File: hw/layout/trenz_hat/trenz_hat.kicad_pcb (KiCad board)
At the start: 2 copper layers, 87 parts

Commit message: Expose Trenz GPIOs on the Pi-outline HDI sensor HAT
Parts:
- added J86: , elec:TZ_FFC40, F.Cu at (0.00, 0.00)
- added J87: , elec:TZ_FFC40, F.Cu at (10.0, 0.00)
- added J88: , elec:TZ_FFC60, F.Cu at (20.0, 0.00)
- added J89: , elec:TZ_FFC60, F.Cu at (30.0, 0.00)
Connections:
- J80 pad 100: 100 -> FPGA_B14_L24_N
- J80 pad 11: GND -> 11
- J80 pad 15: 15 -> FPGA_B13_L6_N
- J80 pad 17: 17 -> FPGA_B13_L6_P
- J80 pad 18: 18 -> FPGA_B13_L3_P
- J80 pad 20: 20 -> FPGA_B13_L3_N
- J80 pad 21: 21 -> FPGA_B13_L5_N
- J80 pad 22: 22 -> FPGA_B13_L11_N
- J80 pad 23: 23 -> FPGA_B13_L5_P
- J80 pad 24: 24 -> FPGA_B13_L11_P
- J80 pad 25: 25 -> GND
- J80 pad 26: 26 -> FPGA_B13_L9_N
- J80 pad 28: 28 -> FPGA_B13_L9_P
- J80 pad 32: GND -> FPGA_B16_L22_P
- J80 pad 34: 34 -> FPGA_B16_L22_N
- J80 pad 35: j80-35 -> FPGA_B16_L16_P
- J80 pad 36: j80-36 -> FPGA_B16_L24_N
- J80 pad 37: 37 -> FPGA_B16_L16_N
- J80 pad 38: j80-38 -> FPGA_B16_L24_P
- J80 pad 39: 39 -> FPGA_B16_L19_N
- J80 pad 41: 41 -> FPGA_B16_L19_P
- J80 pad 42: 42 -> FPGA_B16_L23_P
- J80 pad 44: 44 -> FPGA_B16_L23_N
- J80 pad 45: 45 -> FPGA_B16_L17_N
- J80 pad 46: 46 -> FPGA_B16_L15_P
- J80 pad 47: 47 -> FPGA_B16_L17_P
- J80 pad 48: 48 -> FPGA_B16_L15_N
- J80 pad 49: 49 -> FPGA_B16_L18_N
- J80 pad 50: 50 -> FPGA_B16_L20_P
- J80 pad 51: 51 -> FPGA_B16_L18_P
- J80 pad 52: 52 -> FPGA_B16_L20_N
- J80 pad 55: 55 -> FPGA_B16_L9_N
- J80 pad 56: 56 -> FPGA_B16_L21_P
- J80 pad 57: 57 -> FPGA_B16_L9_P
- J80 pad 58: 58 -> FPGA_B16_L21_N
- J80 pad 59: 59 -> FPGA_B16_L7_N
- J80 pad 60: 60 -> FPGA_B16_L13_P
- J80 pad 61: 61 -> FPGA_B16_L7_P
- J80 pad 62: 62 -> FPGA_B16_L13_N
- J80 pad 65: 65 -> FPGA_B16_L11_P
- J80 pad 66: 66 -> FPGA_B16_L14_P
- J80 pad 67: 67 -> FPGA_B16_L11_N
- J80 pad 68: 68 -> FPGA_B16_L14_N
- J80 pad 69: 69 -> FPGA_B16_L10_N
- J80 pad 7: 7 -> GND
- J80 pad 70: 70 -> FPGA_B16_L3_N
- J80 pad 71: 71 -> FPGA_B16_L10_P
- J80 pad 72: 72 -> FPGA_B16_L3_P
- J80 pad 75: 75 -> FPGA_B16_L5_N
- J80 pad 76: 76 -> FPGA_B16_L12_P
- J80 pad 77: 77 -> FPGA_B16_L5_P
- J80 pad 78: 78 -> FPGA_B16_L12_N
- J80 pad 79: 79 -> FPGA_B16_L2_N
- J80 pad 81: 81 -> FPGA_B16_L2_P
- J80 pad 82: 82 -> FPGA_B16_L8_N
- J80 pad 83: 83 -> GND
- J80 pad 84: 84 -> FPGA_B16_L8_P
- J80 pad 85: 85 -> FPGA_B16_L6_N
- J80 pad 86: 86 -> FPGA_B14_L18_N
- J80 pad 87: 87 -> FPGA_B16_L6_P
- J80 pad 88: 88 -> FPGA_B14_L18_P
- J80 pad 91: 91 -> FPGA_B14_L24_P
- J80 pad 92: 92 -> FPGA_B14_L9_P
- J80 pad 93: 93 -> FPGA_B16_L4_N
- J80 pad 94: 94 -> FPGA_B14_L9_N
- J80 pad 95: 95 -> FPGA_B16_L4_P
- J80 pad 96: 96 -> FPGA_B14_L4_P
- J80 pad 97: 97 -> FPGA_B16_L1_N
- J80 pad 98: 98 -> FPGA_B14_L4_N
- J80 pad 99: 99 -> FPGA_B16_L1_P
- J81 pad 20: j81-20 -> 20
- J81 pad 21: j81-21 -> FPGA_B14_L12_P
- J81 pad 22: j81-22 -> FPGA_B14_L14_P
- J81 pad 23: j81-23 -> FPGA_B14_L12_N
- J81 pad 24: j81-24 -> FPGA_B14_L14_N
- J81 pad 25: j81-25 -> FPGA_B14_L11_P
- J81 pad 26: j81-26 -> FPGA_B14_L13_P
- J81 pad 27: 27 -> FPGA_B14_L11_N
- J81 pad 28: j81-28 -> FPGA_B14_L13_N
- J81 pad 29: GND -> 29
- J81 pad 30: GND -> 30
- J81 pad 31: 31 -> FPGA_B15_L9_N
- J81 pad 32: j81-32 -> FPGA_B14_L16_P
- J81 pad 33: 33 -> FPGA_B15_L9_P
- J81 pad 34: j81-34 -> FPGA_B14_L16_N
- J81 pad 35: j81-35 -> FPGA_B15_L8_N
- J81 pad 36: j81-36 -> FPGA_B14_L15_P
- J81 pad 37: j81-37 -> FPGA_B15_L8_P
- J81 pad 38: j81-38 -> FPGA_B14_L15_N
- J81 pad 41: j81-41 -> FPGA_B15_L7_N
- J81 pad 42: j81-42 -> FPGA_B15_L23_P
- J81 pad 43: 43 -> FPGA_B15_L7_P
- J81 pad 44: j81-44 -> FPGA_B15_L23_N
- J81 pad 45: j81-45 -> FPGA_B15_L13_P
- J81 pad 46: j81-46 -> FPGA_B15_L19_P
- J81 pad 47: j81-47 -> FPGA_B15_L13_N
- J81 pad 48: j81-48 -> FPGA_B15_L19_N
- J81 pad 51: j81-51 -> FPGA_B15_L14_P
- J81 pad 52: j81-52 -> FPGA_B15_L11_P
- J81 pad 53: 53 -> FPGA_B15_L14_N
- J81 pad 54: 54 -> FPGA_B15_L11_N
- J81 pad 55: j81-55 -> FPGA_B15_L12_P
- J81 pad 56: j81-56 -> FPGA_B15_L3_P
- J81 pad 57: j81-57 -> FPGA_B15_L12_N
- J81 pad 58: j81-58 -> FPGA_B15_L3_N
- J81 pad 61: j81-61 -> FPGA_B15_L10_N
- J81 pad 62: j81-62 -> FPGA_B15_L17_N
- J81 pad 63: 63 -> FPGA_B15_L10_P
- J81 pad 64: 64 -> FPGA_B15_L17_P
- J81 pad 65: j81-65 -> FPGA_B15_L18_P
- J81 pad 66: j81-66 -> FPGA_B15_L16_P
- J81 pad 67: j81-67 -> FPGA_B15_L18_N
- J81 pad 68: j81-68 -> FPGA_B15_L16_N
- J81 pad 71: j81-71 -> FPGA_B15_L20_P
- J81 pad 72: j81-72 -> FPGA_B15_L1_P
- J81 pad 73: 73 -> FPGA_B15_L20_N
- J81 pad 74: 74 -> FPGA_B15_L1_N
- J81 pad 75: j81-75 -> FPGA_B15_L15_P
- J81 pad 76: j81-76 -> FPGA_B15_L2_N
- J81 pad 77: j81-77 -> FPGA_B15_L15_N
- J81 pad 78: j81-78 -> FPGA_B15_L2_P
- J81 pad 81: j81-81 -> FPGA_B15_L6_N
- J81 pad 82: j81-82 -> FPGA_B15_L4_P
- J81 pad 83: j81-83 -> FPGA_B15_L6_P
- J81 pad 84: j81-84 -> FPGA_B15_L4_N
- J81 pad 85: j81-85 -> FPGA_B15_L21_P
- J81 pad 86: j81-86 -> FPGA_B15_L5_N
- J81 pad 87: j81-87 -> FPGA_B15_L21_N
- J81 pad 88: j81-88 -> FPGA_B15_L5_P
- J81 pad 90: 90 -> FPGA_B15_IO0
- J81 pad 91: j81-91 -> FPGA_B15_L24_N
- J81 pad 93: j81-93 -> FPGA_B15_L24_P
- J81 pad 95: j81-95 -> FPGA_B15_L22_N
- J81 pad 97: j81-97 -> FPGA_B15_L22_P
- J81 pad 99: j81-99 -> FPGA_B15_IO25
- J82 pad 1: 1 -> FPGA_B13_L14_P
- J82 pad 15: j82-15 -> 15
- J82 pad 2: 2 -> FPGA_B13_L17_P
- J82 pad 21: j82-21 -> 21
- J82 pad 22: j82-22 -> 22
- J82 pad 25: j82-25 -> 25
- J82 pad 26: j82-26 -> 26
- J82 pad 27: j82-27 -> 27
- J82 pad 28: j82-28 -> 28
- J82 pad 3: j82-3 -> FPGA_B13_L14_N
- J82 pad 31: j82-31 -> 31
- J82 pad 33: j82-33 -> 33
- J82 pad 34: j82-34 -> 34
- J82 pad 37: j82-37 -> FPGA_B13_L16_P
- J82 pad 38: j82-38 -> FPGA_B13_L10_P
- J82 pad 39: j82-39 -> FPGA_B13_L16_N
- J82 pad 4: 4 -> FPGA_B13_L17_N
- J82 pad 40: j82-40 -> FPGA_B13_L10_N
- J82 pad 41: j82-41 -> FPGA_B13_L1_P
- J82 pad 42: j82-42 -> FPGA_B13_L15_P
- J82 pad 43: j82-43 -> FPGA_B13_L1_N
- J82 pad 44: j82-44 -> FPGA_B13_L15_N
- J82 pad 47: j82-47 -> FPGA_B13_L4_P
- J82 pad 48: j82-48 -> FPGA_B14_L5_P
- J82 pad 49: j82-49 -> FPGA_B13_L4_N
- J82 pad 50: j82-50 -> FPGA_B14_L5_N
- J82 pad 51: j82-51 -> FPGA_B13_L2_N
- J82 pad 52: j82-52 -> FPGA_B14_L20_P
- J82 pad 53: j82-53 -> FPGA_B13_L2_P
- J82 pad 54: j82-54 -> FPGA_B14_L20_N
- J82 pad 55: j82-55 -> 55
- J82 pad 56: j82-56 -> 56
- J82 pad 57: j82-57 -> FPGA_B13_L12_P
- J82 pad 58: j82-58 -> FPGA_B13_L13_P
- J82 pad 59: j82-59 -> FPGA_B13_L12_N
- J82 pad 60: j82-60 -> FPGA_B13_L13_N
- J82 pad 7: j82-7 -> 7
- U11 pad 11: 11 -> u11-11
- U21 pad 18: u21-18 -> 18
- U21 pad 2: u21-2 -> 2

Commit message: Replace T1 GNSS with single Racotech geophone input
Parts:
- removed C24, C26: , elec:Capacitor_SMD__C_0603_1608Metric
- removed C25: , elec:Capacitor_SMD__C_0805_2012Metric
- removed J2: , elec:Connector_Coaxial__U.FL_Hirose_U.FL-R-SMT-1_Vertical
- removed U21: , elec:RF_GPS__ublox_MAX
- added C90: , elec:Capacitor_SMD__C_1206_3216Metric, F.Cu at (50.0, 0.00)
- added C91: , elec:Capacitor_SMD__C_0603_1608Metric, F.Cu at (60.0, 0.00)
- added C92: , elec:Capacitor_SMD__C_0603_1608Metric, F.Cu at (70.0, 0.00)
- added C93: , elec:Capacitor_SMD__C_0805_2012Metric, F.Cu at (120.0, 0.00)
- added C94: , elec:Capacitor_SMD__C_0805_2012Metric, F.Cu at (140.0, 0.00)
- added C95: , elec:Capacitor_SMD__C_0603_1608Metric, F.Cu at (150.0, 0.00)
- added C96: , elec:Capacitor_SMD__C_0603_1608Metric, F.Cu at (160.0, 0.00)
- added D90: , elec:Package_TO_SOT_SMD__SOT-323_SC-70, F.Cu at (20.0, 0.00)
- added J90: , elec:Connector_Phoenix_MC__PhoenixContact_MCV_1,5_3-G-3.81_1x03_P3.81mm_Vertical, F.Cu at (10.0, 0.00)
- added R90: , elec:Resistor_SMD__R_0603_1608Metric, F.Cu at (30.0, 0.00)
- added R91: , elec:Resistor_SMD__R_0603_1608Metric, F.Cu at (40.0, 0.00)
- added R92: , elec:Resistor_SMD__R_0603_1608Metric, F.Cu at (80.0, 0.00)
- added R93: , elec:Resistor_SMD__R_0603_1608Metric, F.Cu at (90.0, 0.00)
- added R94: , elec:Resistor_SMD__R_0603_1608Metric, F.Cu at (100.0, 0.00)
- added R95: , elec:Resistor_SMD__R_0603_1608Metric, F.Cu at (110.0, 0.00)
- added R96: , elec:Resistor_SMD__R_0603_1608Metric, F.Cu at (130.0, 0.00)
- added R97: , elec:Resistor_SMD__R_0603_1608Metric, F.Cu at (170.0, 0.00)
- added U22: , elec:Package_SO__TSSOP-16_4.4x5mm_P0.65mm, F.Cu at (0.00, 0.00)
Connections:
- net PI_GNSS_PPS renamed PI_GEO_DRDY_N
- U42 pad 16: GNSS_PPS -> GEO_DRDY_N

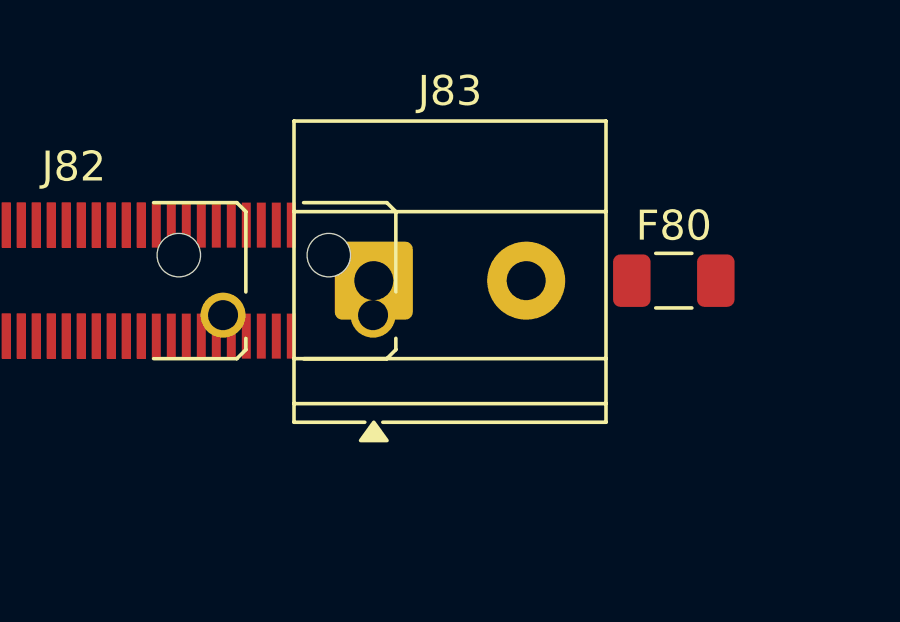
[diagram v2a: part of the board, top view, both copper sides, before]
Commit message: Resolve T1 ribbon clearance with guided flex and windowed support
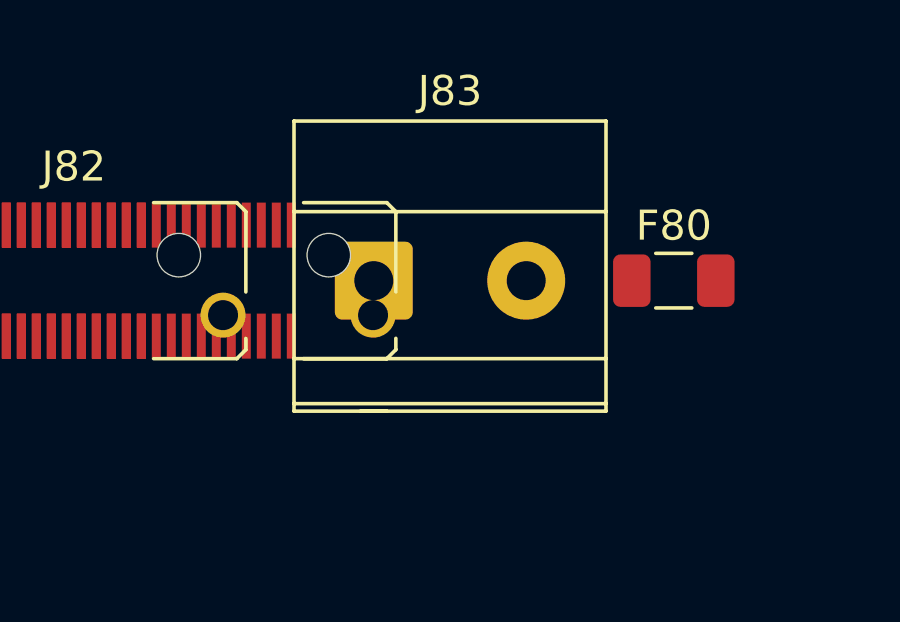
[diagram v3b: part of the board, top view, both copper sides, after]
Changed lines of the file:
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@@
 		)
 		(fp_line
-			(start -2.66 4.72)
-			(end -2.66 -5.32)
-			(stroke
-				(width 0.12)
-				(type solid)
-			)
-			(layer "F.SilkS")
-		)
-		(fp_line
-			(start -0.3 4.72)
-			(end -2.66 4.72)
-			(stroke
-				(width 0.12)
-				(type solid)
-			)
-			(layer "F.SilkS")
-		)
-		(fp_line
-			(start 7.74 -5.32)
-			(end 7.74 4.72)
-			(stroke
-				(width 0.12)
-				(type solid)
-			)
-			(layer "F.SilkS")
-		)
-		(fp_line
-			(start 7.74 4.72)
-			(end 0.3 4.72)
-			(stroke
-				(width 0.12)
-				(type solid)
-			)
-			(layer "F.SilkS")
-		)
-		(fp_line
 			(start -2.54 -5.2)
 			(end 7.62 -5.2)
@@
 			(layer "F.Fab")
 		)
+		(fp_line
+			(start -2.66 4.35)
+			(end -2.66 -5.32)
+			(stroke
+				(width 0.12)
+				(type solid)
+			)
+			(layer "F.SilkS")
+		)
+		(fp_line
+			(start -0.3 4.35)
+			(end -2.66 4.35)
+			(stroke
+				(width 0.12)
+				(type solid)
+			)
+			(layer "F.SilkS")
+		)
+		(fp_line
+			(start 7.74 -5.32)
+			(end 7.74 4.35)
+			(stroke
+				(width 0.12)
+				(type solid)
+			)
+			(layer "F.SilkS")
+		)
+		(fp_line
+			(start 7.74 4.35)
+			(end 0.3 4.35)
+			(stroke
+				(width 0.12)
+				(type solid)
+			)
+			(layer "F.SilkS")
+		)
 		(fp_circle
 			(center 0 0)
@@
 		(fp_poly
 			(pts
-				(xy 0 4.72) (xy 0.44 5.33) (xy -0.44 5.33)
+				(xy 0 4.35) (xy 0.44 4.35) (xy -0.44 4.35)
 			)
 			(stroke
@@
 		)
 		(pad "1" smd roundrect
-			(at -2.8625 -2.275 0)
+			(at -2.8625 -2.275)
 			(size 1.475 0.4)
 			(layers "F.Cu" "F.Mask" "F.Paste")
@@
 		)
 		(pad "2" smd roundrect
-			(at -2.8625 -1.625 0)
+			(at -2.8625 -1.625)
 			(size 1.475 0.4)
 			(layers "F.Cu" "F.Mask" "F.Paste")
@@
 		)
 		(pad "3" smd roundrect
-			(at -2.8625 -0.975 0)
+			(at -2.8625 -0.975)
 			(size 1.475 0.4)
 			(layers "F.Cu" "F.Mask" "F.Paste")
@@
 		)
 		(pad "4" smd roundrect
-			(at -2.8625 -0.325 0)
+			(at -2.8625 -0.325)
 			(size 1.475 0.4)
 			(layers "F.Cu" "F.Mask" "F.Paste")
@@
 		)
 		(pad "5" smd roundrect
-			(at -2.8625 0.325 0)
+			(at -2.8625 0.325)
 			(size 1.475 0.4)
 			(layers "F.Cu" "F.Mask" "F.Paste")
@@
 		)
 		(pad "6" smd roundrect
-			(at -2.8625 0.975 0)
+			(at -2.8625 0.975)
 			(size 1.475 0.4)
 			(layers "F.Cu" "F.Mask" "F.Paste")
@@
 		)
 		(pad "7" smd roundrect
-			(at -2.8625 1.625 0)
+			(at -2.8625 1.625)
 			(size 1.475 0.4)
 			(layers "F.Cu" "F.Mask" "F.Paste")
@@
 		)
 		(pad "8" smd roundrect
-			(at -2.8625 2.275 0)
+			(at -2.8625 2.275)
 			(size 1.475 0.4)
 			(layers "F.Cu" "F.Mask" "F.Paste")
@@
 		)
 		(pad "9" smd roundrect
-			(at 2.8625 2.275 0)
+			(at 2.8625 2.275)
 			(size 1.475 0.4)
 			(layers "F.Cu" "F.Mask" "F.Paste")
@@
 		)
 		(pad "10" smd roundrect
-			(at 2.8625 1.625 0)
+			(at 2.8625 1.625)
 			(size 1.475 0.4)
 			(layers "F.Cu" "F.Mask" "F.Paste")
@@
 		)
 		(pad "11" smd roundrect
-			(at 2.8625 0.975 0)
+			(at 2.8625 0.975)
 			(size 1.475 0.4)
 			(layers "F.Cu" "F.Mask" "F.Paste")
@@
 		)
 		(pad "12" smd roundrect
-			(at 2.8625 0.325 0)
+			(at 2.8625 0.325)
 			(size 1.475 0.4)
 			(layers "F.Cu" "F.Mask" "F.Paste")
@@
 		)
 		(pad "13" smd roundrect
-			(at 2.8625 -0.325 0)
+			(at 2.8625 -0.325)
 			(size 1.475 0.4)
 			(layers "F.Cu" "F.Mask" "F.Paste")
@@
 		)
 		(pad "14" smd roundrect
-			(at 2.8625 -0.975 0)
+			(at 2.8625 -0.975)
 			(size 1.475 0.4)
 			(layers "F.Cu" "F.Mask" "F.Paste")
@@
 		)
 		(pad "15" smd roundrect
-			(at 2.8625 -1.625 0)
+			(at 2.8625 -1.625)
 			(size 1.475 0.4)
 			(layers "F.Cu" "F.Mask" "F.Paste")
@@
 		)
 		(pad "16" smd roundrect
-			(at 2.8625 -2.275 0)
+			(at 2.8625 -2.275)
 			(size 1.475 0.4)
 			(layers "F.Cu" "F.Mask" "F.Paste")
@@
 		)
 		(pad "1" thru_hole roundrect
-			(at 0 0 0)
+			(at 0 0)
 			(size 1.8 3.6)
 			(drill 1.2)
@@
 		)
 		(pad "2" thru_hole oval
-			(at 3.81 0 0)
+			(at 3.81 0)
 			(size 1.8 3.6)
 			(drill 1.2)
@@
 		)
 		(pad "3" thru_hole oval
-			(at 7.62 0 0)
+			(at 7.62 0)
 			(size 1.8 3.6)
 			(drill 1.2)
@@
 		)
 		(pad "1" smd roundrect
-			(at -0.9375 -0.65 0)
+			(at -0.9375 -0.65)
 			(size 1.225 0.5)
 			(layers "F.Cu" "F.Mask" "F.Paste")
@@
 		)
 		(pad "2" smd roundrect
-			(at -0.9375 0.65 0)
+			(at -0.9375 0.65)
 			(size 1.225 0.5)
 			(layers "F.Cu" "F.Mask" "F.Paste")
@@
 		)
 		(pad "3" smd roundrect
-			(at 0.9375 0 0)
+			(at 0.9375 0)
 			(size 1.225 0.5)
 			(layers "F.Cu" "F.Mask" "F.Paste")
@@
 		)
 		(pad "1" smd roundrect
-			(at -0.825 0 0)
+			(at -0.825 0)
 			(size 0.8 0.95)
 			(layers "F.Cu" "F.Mask" "F.Paste")
@@
 		)
 		(pad "2" smd roundrect
-			(at 0.825 0 0)
+			(at 0.825 0)
 			(size 0.8 0.95)
 			(layers "F.Cu" "F.Mask" "F.Paste")
@@
 		)
 		(pad "1" smd roundrect
-			(at -0.825 0 0)
+			(at -0.825 0)
 			(size 0.8 0.95)
 			(layers "F.Cu" "F.Mask" "F.Paste")
@@
 		)
 		(pad "2" smd roundrect
-			(at 0.825 0 0)
+			(at 0.825 0)
 			(size 0.8 0.95)
 			(layers "F.Cu" "F.Mask" "F.Paste")
@@
 		)
 		(pad "1" smd roundrect
-			(at -1.475 0 0)
+			(at -1.475 0)
 			(size 1.15 1.8)
 			(layers "F.Cu" "F.Mask" "F.Paste")
@@
 		)
 		(pad "2" smd roundrect
-			(at 1.475 0 0)
+			(at 1.475 0)
 			(size 1.15 1.8)
 			(layers "F.Cu" "F.Mask" "F.Paste")
@@
 		)
 		(pad "1" smd roundrect
-			(at -0.775 0 0)
+			(at -0.775 0)
 			(size 0.9 0.95)
 			(layers "F.Cu" "F.Mask" "F.Paste")
@@
 		)
 		(pad "2" smd roundrect
-			(at 0.775 0 0)
+			(at 0.775 0)
 			(size 0.9 0.95)
 			(layers "F.Cu" "F.Mask" "F.Paste")
@@
 		)
 		(pad "1" smd roundrect
-			(at -0.775 0 0)
+			(at -0.775 0)
 			(size 0.9 0.95)
 			(layers "F.Cu" "F.Mask" "F.Paste")
@@
 		)
 		(pad "2" smd roundrect
-			(at 0.775 0 0)
+			(at 0.775 0)
 			(size 0.9 0.95)
 			(layers "F.Cu" "F.Mask" "F.Paste")
@@
 		)
 		(pad "1" smd roundrect
-			(at -0.825 0 0)
+			(at -0.825 0)
 			(size 0.8 0.95)
 			(layers "F.Cu" "F.Mask" "F.Paste")
@@
 		)
 		(pad "2" smd roundrect
-			(at 0.825 0 0)
+			(at 0.825 0)
 			(size 0.8 0.95)
 			(layers "F.Cu" "F.Mask" "F.Paste")
@@
 		)
 		(pad "1" smd roundrect
-			(at -0.825 0 0)
+			(at -0.825 0)
 			(size 0.8 0.95)
 			(layers "F.Cu" "F.Mask" "F.Paste")
@@
 		)
 		(pad "2" smd roundrect
-			(at 0.825 0 0)
+			(at 0.825 0)
 			(size 0.8 0.95)
 			(layers "F.Cu" "F.Mask" "F.Paste")
@@
 		)
 		(pad "1" smd roundrect
-			(at -0.825 0 0)
+			(at -0.825 0)
 			(size 0.8 0.95)
 			(layers "F.Cu" "F.Mask" "F.Paste")
@@
 		)
 		(pad "2" smd roundrect
-			(at 0.825 0 0)
+			(at 0.825 0)
 			(size 0.8 0.95)
 			(layers "F.Cu" "F.Mask" "F.Paste")
@@
 		)
 		(pad "1" smd roundrect
-			(at -0.825 0 0)
+			(at -0.825 0)
 			(size 0.8 0.95)
 			(layers "F.Cu" "F.Mask" "F.Paste")
@@
 		)
 		(pad "2" smd roundrect
-			(at 0.825 0 0)
+			(at 0.825 0)
 			(size 0.8 0.95)
 			(layers "F.Cu" "F.Mask" "F.Paste")
@@
 		)
 		(pad "1" smd roundrect
-			(at -0.95 0 0)
+			(at -0.95 0)
 			(size 1 1.45)
 			(layers "F.Cu" "F.Mask" "F.Paste")
@@
 		)
 		(pad "2" smd roundrect
-			(at 0.95 0 0)
+			(at 0.95 0)
 			(size 1 1.45)
 			(layers "F.Cu" "F.Mask" "F.Paste")
@@
 		)
 		(pad "1" smd roundrect
-			(at -0.825 0 0)
+			(at -0.825 0)
 			(size 0.8 0.95)
 			(layers "F.Cu" "F.Mask" "F.Paste")
@@
 		)
 		(pad "2" smd roundrect
-			(at 0.825 0 0)
+			(at 0.825 0)
 			(size 0.8 0.95)
 			(layers "F.Cu" "F.Mask" "F.Paste")
@@
 		)
 		(pad "1" smd roundrect
-			(at -0.95 0 0)
+			(at -0.95 0)
 			(size 1 1.45)
 			(layers "F.Cu" "F.Mask" "F.Paste")
@@
 		)
 		(pad "2" smd roundrect
-			(at 0.95 0 0)
+			(at 0.95 0)
 			(size 1 1.45)
 			(layers "F.Cu" "F.Mask" "F.Paste")
@@
 		)
 		(pad "1" smd roundrect
-			(at -0.775 0 0)
+			(at -0.775 0)
 			(size 0.9 0.95)
 			(layers "F.Cu" "F.Mask" "F.Paste")
@@
 		)
 		(pad "2" smd roundrect
-			(at 0.775 0 0)
+			(at 0.775 0)
 			(size 0.9 0.95)
 			(layers "F.Cu" "F.Mask" "F.Paste")
@@
 		)
 		(pad "1" smd roundrect
-			(at -0.775 0 0)
+			(at -0.775 0)
 			(size 0.9 0.95)
 			(layers "F.Cu" "F.Mask" "F.Paste")
@@
 		)
 		(pad "2" smd roundrect
-			(at 0.775 0 0)
+			(at 0.775 0)
 			(size 0.9 0.95)
 			(layers "F.Cu" "F.Mask" "F.Paste")
@@
 		)
 		(pad "1" smd roundrect
-			(at -0.825 0 0)
+			(at -0.825 0)
 			(size 0.8 0.95)
 			(layers "F.Cu" "F.Mask" "F.Paste")
@@
 		)
 		(pad "2" smd roundrect
-			(at 0.825 0 0)
+			(at 0.825 0)
 			(size 0.8 0.95)
 			(layers "F.Cu" "F.Mask" "F.Paste")
